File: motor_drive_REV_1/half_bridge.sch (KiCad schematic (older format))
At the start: 28 parts

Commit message: work on component libraries and schematic
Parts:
- removed Q? (x8): Q_NMOS_DGS, symbol Device:Q_NMOS_DGS
- removed R? (x16): 6.8, symbol Device:R
- removed R? (x4): R, symbol Device:R
- added Q? (x2): nmos, symbol motor_drive:nmos
- added R? (x2): R, symbol motor_drive:R
- added R?: R_Shunt, symbol motor_drive:R_Shunt
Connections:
- net labels added: DC_neg, DC_pos
- net labels removed: DC+, DC-, SL, V_sense_n, V_sense_p
- wire segments 26 -> 16

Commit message: organizing pinout and BOM
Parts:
- removed R?: R_Shunt, symbol motor_drive:R_Shunt
- added R3: R, motor_drive_footprints:C_0603_1608Metric, symbol motor_drive:R
- Q1, Q2: renamed from Q?; footprint (none) -> motor_drive_footprints:NTTGS5820NL-D
- R1, R2: renamed from R?; footprint (none) -> motor_drive_footprints:C_0603_1608Metric
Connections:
- wire segments 16 -> 15
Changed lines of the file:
@@
 $Descr A4 11693 8268
 encoding utf-8
-Sheet 3 14
+Sheet 4 14
 Title ""
 Date ""
@@
 Comment4 ""
 $EndDescr
-Wire Wire Line
-	5100 3600 5100 3700
 Connection ~ 5100 3700
 Wire Wire Line
@@
 Text HLabel 5750 3400 1    50   Input ~ 0
 I_sense_p
-Text HLabel 5950 3400 1    50   Input ~ 0
+Text HLabel 6050 3400 1    50   Input ~ 0
 I_sense_n
-Text HLabel 4200 3400 0    50   Input ~ 0
-GH
 Text HLabel 4200 4000 0    50   Input ~ 0
 GL
@@
 Wire Wire Line
 	4200 3700 5100 3700
-Wire Wire Line
-	4250 4000 4400 4000
 Text HLabel 6750 3700 2    50   Input ~ 0
 M
 Text HLabel 5750 3400 1    50   Input ~ 0
 I_sense_p
-Text HLabel 5950 3400 1    50   Input ~ 0
+Text HLabel 6050 3400 1    50   Input ~ 0
 I_sense_n
-Text HLabel 4200 3400 0    50   Input ~ 0
-GH
 Text HLabel 4200 4000 0    50   Input ~ 0
 GL
@@
 Text HLabel 5750 3400 1    50   Input ~ 0
 I_sense_p
-Text HLabel 5950 3400 1    50   Input ~ 0
+Text HLabel 6050 3400 1    50   Input ~ 0
 I_sense_n
-Text HLabel 4200 3400 0    50   Input ~ 0
-GH
 Text HLabel 4200 4000 0    50   Input ~ 0
 GL
@@
 Text HLabel 5750 3400 1    50   Input ~ 0
 I_sense_p
-Text HLabel 5950 3400 1    50   Input ~ 0
+Text HLabel 6050 3400 1    50   Input ~ 0
 I_sense_n
-Text HLabel 4200 3400 0    50   Input ~ 0
-GH
 Text HLabel 4200 4000 0    50   Input ~ 0
 GL
@@
 M
 $Comp
-L motor_drive:nmos Q?
+L motor_drive:nmos Q1
 U 1 1 5E277B3C
 P 5000 3400
-F 0 "Q?" H 5204 3446 50  0000 L CNN
+AR Path="/5E257703/5E277B3C" Ref="Q1"  Part="1"
+AR Path="/5E26944C/5E277B3C" Ref="Q3"  Part="1"
+AR Path="/5E26B60E/5E277B3C" Ref="Q5"  Part="1"
+F 0 "Q5" H 5204 3446 50  0000 L CNN
 F 1 "nmos" H 5204 3355 50  0000 L CNN
-F 2 "" H 5200 3500 50  0001 C CNN
+F 2 "motor_drive_footprints:NTTGS5820NL-D" H 5200 3500 50  0001 C CNN
 F 3 "~" H 5000 3400 50  0001 C CNN
 	1    5000 3400
 	1    0    0    -1
 $EndComp
-Wire Wire Line
-	5100 3650 5100 3700
 $Comp
-L motor_drive:nmos Q?
+L motor_drive:nmos Q2
 U 1 1 5E279347
 P 5000 4000
-F 0 "Q?" H 5204 4046 50  0000 L CNN
+AR Path="/5E257703/5E279347" Ref="Q2"  Part="1"
+AR Path="/5E26944C/5E279347" Ref="Q4"  Part="1"
+AR Path="/5E26B60E/5E279347" Ref="Q6"  Part="1"
+F 0 "Q6" H 5204 4046 50  0000 L CNN
 F 1 "nmos" H 5204 3955 50  0000 L CNN
-F 2 "" H 5200 4100 50  0001 C CNN
+F 2 "motor_drive_footprints:NTTGS5820NL-D" H 5200 4100 50  0001 C CNN
 F 3 "~" H 5000 4000 50  0001 C CNN
 	1    5000 4000
@@
 $EndComp
 $Comp
-L motor_drive:R R?
+L motor_drive:R R2
 U 1 1 5E27A2EF
 P 4550 4000
-F 0 "R?" V 4343 4000 50  0000 C CNN
+AR Path="/5E257703/5E27A2EF" Ref="R2"  Part="1"
+AR Path="/5E26944C/5E27A2EF" Ref="R5"  Part="1"
+AR Path="/5E26B60E/5E27A2EF" Ref="R8"  Part="1"
+F 0 "R8" V 4343 4000 50  0000 C CNN
 F 1 "R" V 4434 4000 50  0000 C CNN
-F 2 "" V 4480 4000 50  0001 C CNN
+F 2 "motor_drive_footprints:C_0603_1608Metric" V 4480 4000 50  0001 C CNN
 F 3 "~" H 4550 4000 50  0001 C CNN
 	1    4550 4000
 	0    1    1    0
 $EndComp
-Wire Wire Line
-	4250 3400 4400 3400
 $Comp
-L motor_drive:R R?
+L motor_drive:R R1
 U 1 1 5E27D5F7
 P 4550 3400
-F 0 "R?" V 4343 3400 50  0000 C CNN
+AR Path="/5E257703/5E27D5F7" Ref="R1"  Part="1"
+AR Path="/5E26944C/5E27D5F7" Ref="R4"  Part="1"
+AR Path="/5E26B60E/5E27D5F7" Ref="R7"  Part="1"
+F 0 "R7" V 4343 3400 50  0000 C CNN
 F 1 "R" V 4434 3400 50  0000 C CNN
-F 2 "" V 4480 3400 50  0001 C CNN
+F 2 "motor_drive_footprints:C_0603_1608Metric" V 4480 3400 50  0001 C CNN
 F 3 "~" H 4550 3400 50  0001 C CNN
 	1    4550 3400
@@
 Wire Wire Line
 	4700 4000 4800 4000
-$Comp
-L motor_drive:R_Shunt R?
-U 1 1 5E27E460
-P 5850 3700
-F 0 "R?" V 5717 3700 50  0000 C CNN
-F 1 "R_Shunt" V 5626 3700 50  0000 C CNN
-F 2 "" V 5780 3700 50  0001 C CNN
-F 3 "~" H 5850 3700 50  0001 C CNN
-	1    5850 3700
-	0    -1   -1   0
-$EndComp
-Wire Wire Line
-	5100 3700 5650 3700
 Wire Wire Line
 	6050 3700 6750 3700
-Wire Wire Line
-	5750 3400 5750 3550
-Wire Wire Line
-	5950 3400 5950 3550
-Text HLabel 4250 4300 0    50   Input ~ 0
+Text HLabel 4200 4300 0    50   Input ~ 0
 DC_neg
-Text HLabel 4250 3100 0    50   Input ~ 0
+Text HLabel 4200 3100 0    50   Input ~ 0
 DC_pos
-Wire Wire Line
-	4250 3100 5100 3100
 Wire Wire Line
 	5100 3100 5100 3200
 Wire Wire Line
-	4250 4300 5100 4300
+	5100 4300 5100 4200
+$Comp
+L motor_drive:R R3
+U 1 1 5E35BEDA
+P 5900 3700
+AR Path="/5E257703/5E35BEDA" Ref="R3"  Part="1"
+AR Path="/5E26944C/5E35BEDA" Ref="R6"  Part="1"
+AR Path="/5E26B60E/5E35BEDA" Ref="R9"  Part="1"
+F 0 "R9" V 5693 3700 50  0000 C CNN
+F 1 "R" V 5784 3700 50  0000 C CNN
+F 2 "motor_drive_footprints:C_0603_1608Metric" V 5830 3700 50  0001 C CNN
+F 3 "~" H 5900 3700 50  0001 C CNN
+	1    5900 3700
+	0    1    1    0
+$EndComp
 Wire Wire Line
-	5100 4300 5100 4200
+	5100 3700 5750 3700
+Wire Wire Line
+	5750 3400 5750 3700
+Connection ~ 5750 3700
+Wire Wire Line
+	6050 3400 6050 3700
+Connection ~ 6050 3700
+Wire Wire Line
+	5100 3700 5100 3600
+Text HLabel 4200 3400 0    50   Input ~ 0
+GH
+Text HLabel 4200 3400 0    50   Input ~ 0
+GH
+Text HLabel 4200 3400 0    50   Input ~ 0
+GH
+Text HLabel 4200 3400 0    50   Input ~ 0
+GH
+Wire Wire Line
+	4200 3400 4400 3400
+Wire Wire Line
+	4200 4000 4400 4000
+Wire Wire Line
+	4200 3100 5100 3100
+Wire Wire Line
+	4200 4300 5100 4300
 $EndSCHEMATC

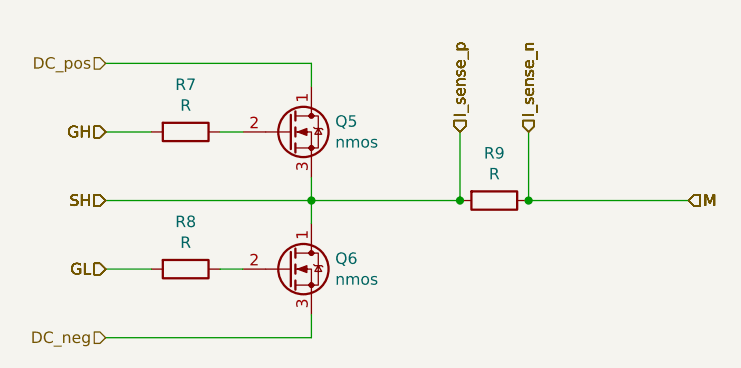
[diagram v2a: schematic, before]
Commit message: working on adding thermistors but encountered too many hierarchicaly copies bug
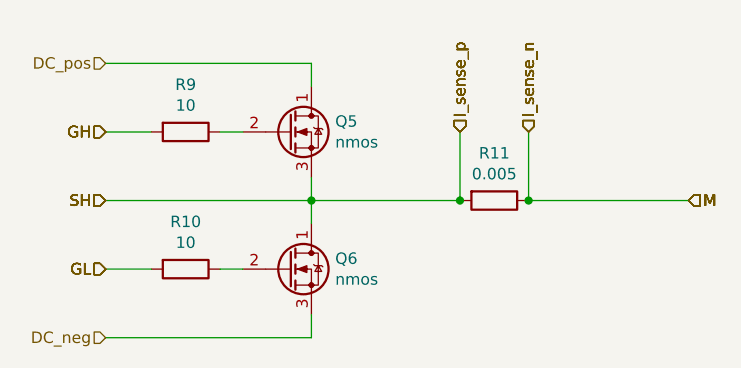
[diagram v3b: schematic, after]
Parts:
- R3: renamed from R1; value R -> 10
- R4: renamed from R2; value R -> 10
- R5: renamed from R3; value R -> 0.005
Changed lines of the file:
@@
 $EndComp
 $Comp
-L motor_drive:R R2
+L motor_drive:R R4
 U 1 1 5E27A2EF
 P 4550 4000
-AR Path="/5E257703/5E27A2EF" Ref="R2"  Part="1"
-AR Path="/5E26944C/5E27A2EF" Ref="R5"  Part="1"
-AR Path="/5E26B60E/5E27A2EF" Ref="R8"  Part="1"
-F 0 "R8" V 4343 4000 50  0000 C CNN
-F 1 "R" V 4434 4000 50  0000 C CNN
+AR Path="/5E257703/5E27A2EF" Ref="R4"  Part="1"
+AR Path="/5E26944C/5E27A2EF" Ref="R7"  Part="1"
+AR Path="/5E26B60E/5E27A2EF" Ref="R10"  Part="1"
+F 0 "R10" V 4343 4000 50  0000 C CNN
+F 1 "10" V 4434 4000 50  0000 C CNN
 F 2 "motor_drive_footprints:C_0603_1608Metric" V 4480 4000 50  0001 C CNN
 F 3 "~" H 4550 4000 50  0001 C CNN
@@
 $EndComp
 $Comp
-L motor_drive:R R1
+L motor_drive:R R3
 U 1 1 5E27D5F7
 P 4550 3400
-AR Path="/5E257703/5E27D5F7" Ref="R1"  Part="1"
-AR Path="/5E26944C/5E27D5F7" Ref="R4"  Part="1"
-AR Path="/5E26B60E/5E27D5F7" Ref="R7"  Part="1"
-F 0 "R7" V 4343 3400 50  0000 C CNN
-F 1 "R" V 4434 3400 50  0000 C CNN
+AR Path="/5E257703/5E27D5F7" Ref="R3"  Part="1"
+AR Path="/5E26944C/5E27D5F7" Ref="R6"  Part="1"
+AR Path="/5E26B60E/5E27D5F7" Ref="R9"  Part="1"
+F 0 "R9" V 4343 3400 50  0000 C CNN
+F 1 "10" V 4434 3400 50  0000 C CNN
 F 2 "motor_drive_footprints:C_0603_1608Metric" V 4480 3400 50  0001 C CNN
 F 3 "~" H 4550 3400 50  0001 C CNN
@@
 	5100 4300 5100 4200
 $Comp
-L motor_drive:R R3
+L motor_drive:R R5
 U 1 1 5E35BEDA
 P 5900 3700
-AR Path="/5E257703/5E35BEDA" Ref="R3"  Part="1"
-AR Path="/5E26944C/5E35BEDA" Ref="R6"  Part="1"
-AR Path="/5E26B60E/5E35BEDA" Ref="R9"  Part="1"
-F 0 "R9" V 5693 3700 50  0000 C CNN
-F 1 "R" V 5784 3700 50  0000 C CNN
+AR Path="/5E257703/5E35BEDA" Ref="R5"  Part="1"
+AR Path="/5E26944C/5E35BEDA" Ref="R8"  Part="1"
+AR Path="/5E26B60E/5E35BEDA" Ref="R11"  Part="1"
+F 0 "R11" V 5693 3700 50  0000 C CNN
+F 1 "0.005" V 5784 3700 50  0000 C CNN
 F 2 "motor_drive_footprints:C_0603_1608Metric" V 5830 3700 50  0001 C CNN
 F 3 "~" H 5900 3700 50  0001 C CNN

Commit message: started layout
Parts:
- removed R5: 0.005, motor_drive_footprints:C_0603_1608Metric, symbol motor_drive:R
- added R6: WSL20101L000FEA18, motor_drive_footprints:WSL20101L000FEA18, symbol motor_drive:WSL20101L000FEA18
- renumbered R3 to R1, R4 to R2
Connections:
- net I_sense_n: now also R6.1
- net I_sense_p: now also R6.2
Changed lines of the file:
@@
 $Descr A4 11693 8268
 encoding utf-8
-Sheet 4 14
+Sheet 4 16
 Title ""
 Date ""
@@
 Text HLabel 5750 3400 1    50   Input ~ 0
 I_sense_p
-Text HLabel 6050 3400 1    50   Input ~ 0
+Text HLabel 6250 3400 1    50   Input ~ 0
 I_sense_n
 Text HLabel 4200 4000 0    50   Input ~ 0
@@
 Wire Wire Line
 	4200 3700 5100 3700
-Text HLabel 6750 3700 2    50   Input ~ 0
+Text HLabel 6950 3700 2    50   Input ~ 0
 M
 Text HLabel 5750 3400 1    50   Input ~ 0
 I_sense_p
-Text HLabel 6050 3400 1    50   Input ~ 0
+Text HLabel 6250 3400 1    50   Input ~ 0
 I_sense_n
 Text HLabel 4200 4000 0    50   Input ~ 0
@@
 Text HLabel 4200 3700 0    50   Input ~ 0
 SH
-Text HLabel 6750 3700 2    50   Input ~ 0
+Text HLabel 6950 3700 2    50   Input ~ 0
 M
 Text HLabel 5750 3400 1    50   Input ~ 0
 I_sense_p
-Text HLabel 6050 3400 1    50   Input ~ 0
+Text HLabel 6250 3400 1    50   Input ~ 0
 I_sense_n
 Text HLabel 4200 4000 0    50   Input ~ 0
@@
 Text HLabel 4200 3700 0    50   Input ~ 0
 SH
-Text HLabel 6750 3700 2    50   Input ~ 0
+Text HLabel 6950 3700 2    50   Input ~ 0
 M
 Text HLabel 5750 3400 1    50   Input ~ 0
 I_sense_p
-Text HLabel 6050 3400 1    50   Input ~ 0
+Text HLabel 6250 3400 1    50   Input ~ 0
 I_sense_n
 Text HLabel 4200 4000 0    50   Input ~ 0
@@
 Text HLabel 4200 3700 0    50   Input ~ 0
 SH
-Text HLabel 6750 3700 2    50   Input ~ 0
+Text HLabel 6950 3700 2    50   Input ~ 0
 M
 $Comp
@@
 $EndComp
 $Comp
-L motor_drive:R R4
+L motor_drive:R R2
 U 1 1 5E27A2EF
 P 4550 4000
-AR Path="/5E257703/5E27A2EF" Ref="R4"  Part="1"
-AR Path="/5E26944C/5E27A2EF" Ref="R7"  Part="1"
-AR Path="/5E26B60E/5E27A2EF" Ref="R10"  Part="1"
-F 0 "R10" V 4343 4000 50  0000 C CNN
+AR Path="/5E257703/5E27A2EF" Ref="R2"  Part="1"
+AR Path="/5E26944C/5E27A2EF" Ref="R5"  Part="1"
+AR Path="/5E26B60E/5E27A2EF" Ref="R8"  Part="1"
+F 0 "R8" V 4343 4000 50  0000 C CNN
 F 1 "10" V 4434 4000 50  0000 C CNN
 F 2 "motor_drive_footprints:C_0603_1608Metric" V 4480 4000 50  0001 C CNN
@@
 $EndComp
 $Comp
-L motor_drive:R R3
+L motor_drive:R R1
 U 1 1 5E27D5F7
 P 4550 3400
-AR Path="/5E257703/5E27D5F7" Ref="R3"  Part="1"
-AR Path="/5E26944C/5E27D5F7" Ref="R6"  Part="1"
-AR Path="/5E26B60E/5E27D5F7" Ref="R9"  Part="1"
-F 0 "R9" V 4343 3400 50  0000 C CNN
+AR Path="/5E257703/5E27D5F7" Ref="R1"  Part="1"
+AR Path="/5E26944C/5E27D5F7" Ref="R4"  Part="1"
+AR Path="/5E26B60E/5E27D5F7" Ref="R7"  Part="1"
+F 0 "R7" V 4343 3400 50  0000 C CNN
 F 1 "10" V 4434 3400 50  0000 C CNN
 F 2 "motor_drive_footprints:C_0603_1608Metric" V 4480 3400 50  0001 C CNN
@@
 	4700 4000 4800 4000
 Wire Wire Line
-	6050 3700 6750 3700
+	6250 3700 6950 3700
 Text HLabel 4200 4300 0    50   Input ~ 0
 DC_neg
@@
 Wire Wire Line
 	5100 4300 5100 4200
-$Comp
-L motor_drive:R R5
-U 1 1 5E35BEDA
-P 5900 3700
-AR Path="/5E257703/5E35BEDA" Ref="R5"  Part="1"
-AR Path="/5E26944C/5E35BEDA" Ref="R8"  Part="1"
-AR Path="/5E26B60E/5E35BEDA" Ref="R11"  Part="1"
-F 0 "R11" V 5693 3700 50  0000 C CNN
-F 1 "0.005" V 5784 3700 50  0000 C CNN
-F 2 "motor_drive_footprints:C_0603_1608Metric" V 5830 3700 50  0001 C CNN
-F 3 "~" H 5900 3700 50  0001 C CNN
-	1    5900 3700
-	0    1    1    0
-$EndComp
 Wire Wire Line
 	5100 3700 5750 3700
 Wire Wire Line
 	5750 3400 5750 3700
-Connection ~ 5750 3700
 Wire Wire Line
-	6050 3400 6050 3700
-Connection ~ 6050 3700
+	6250 3400 6250 3700
 Wire Wire Line
 	5100 3700 5100 3600
@@
 Wire Wire Line
 	4200 4300 5100 4300
+$Comp
+L motor_drive:WSL20101L000FEA18 R6
+U 1 1 5E424CCF
+P 5750 3700
+AR Path="/5E26944C/5E424CCF" Ref="R6"  Part="1"
+AR Path="/5E257703/5E424CCF" Ref="R3"  Part="1"
+AR Path="/5E26B60E/5E424CCF" Ref="R9"  Part="1"
+F 0 "R9" H 6000 3832 60  0000 C CNN
+F 1 "WSL20101L000FEA18" H 6000 3832 60  0001 C CNN
+F 2 "motor_drive_footprints:WSL20101L000FEA18" H 6000 3365 60  0001 C CNN
+F 3 "" H 5750 3700 60  0000 C CNN
+	1    5750 3700
+	1    0    0    -1
+$EndComp
+Connection ~ 5750 3700
+Connection ~ 6250 3700
 $EndSCHEMATC

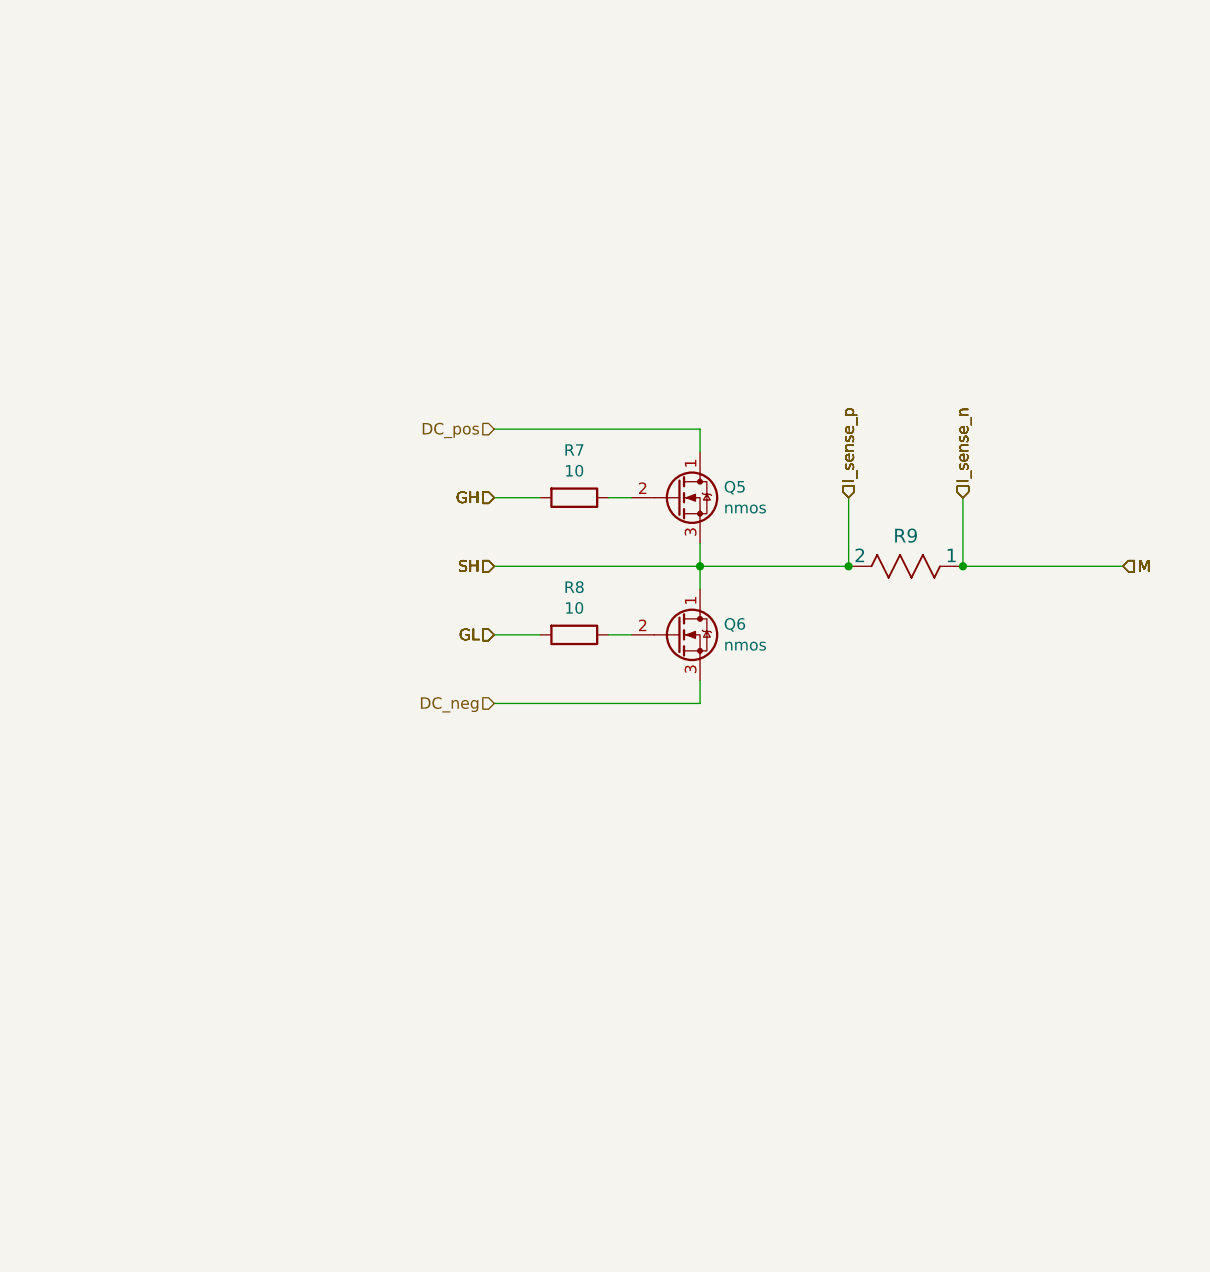
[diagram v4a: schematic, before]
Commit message: gate drive rework and schematic re-organization
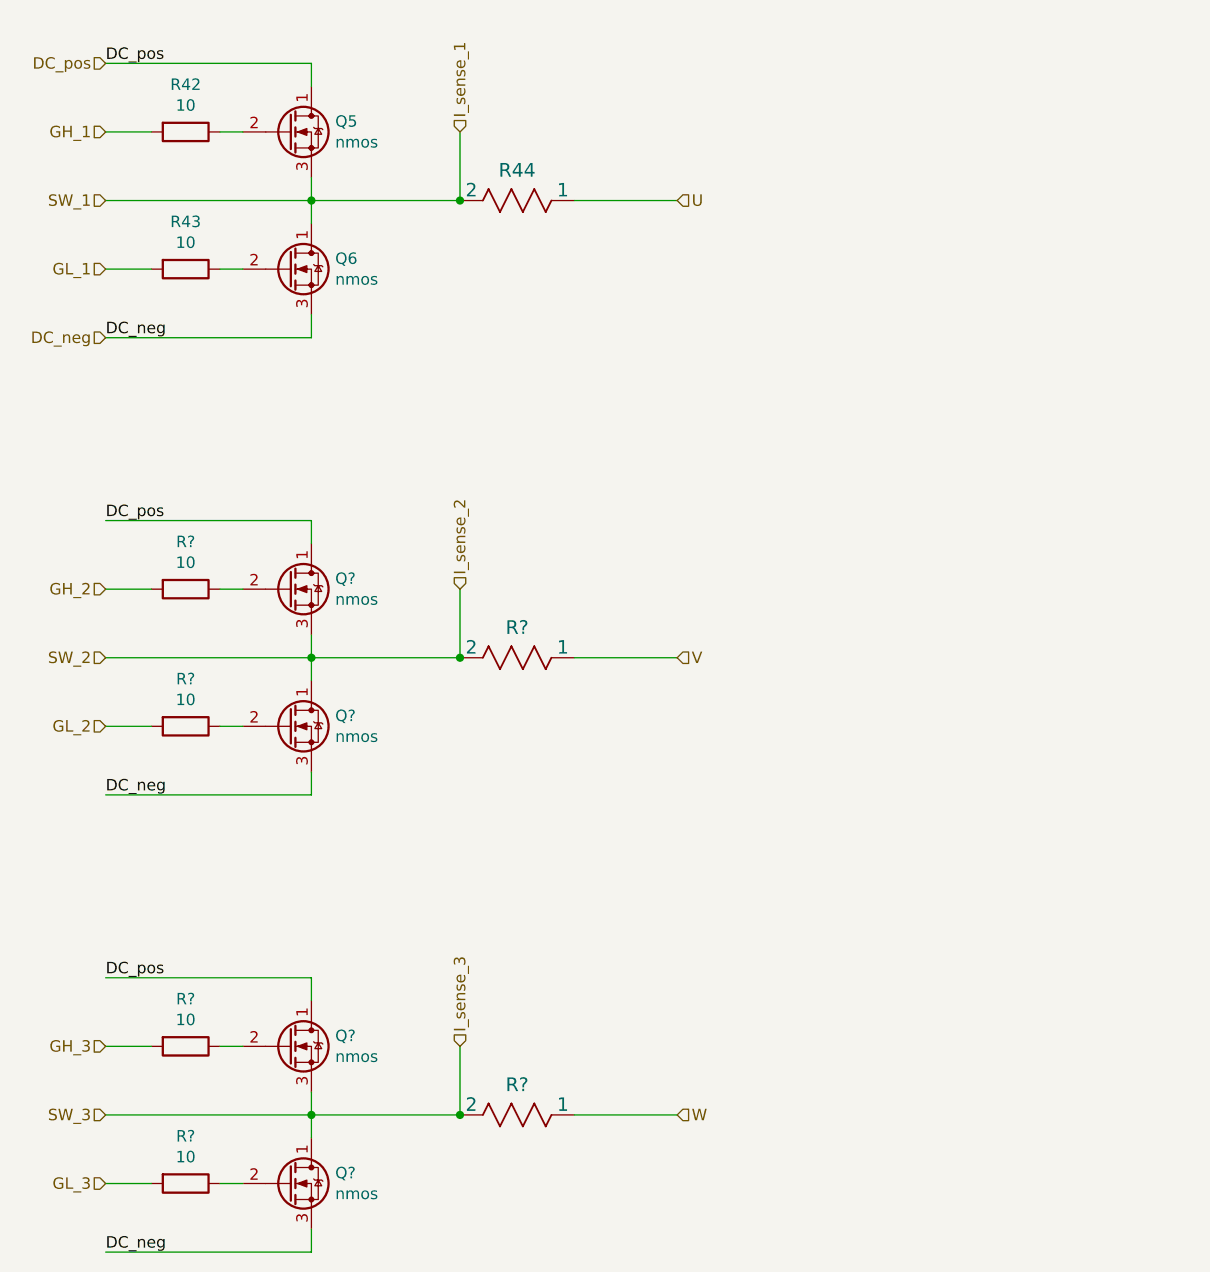
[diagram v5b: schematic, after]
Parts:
- added Q? (x4): nmos, motor_drive_footprints:NTTGS5820NL-D, symbol motor_drive:nmos
- added R? (x4): 10, motor_drive_footprints:C_0603_1608Metric, symbol motor_drive:R
- added R? (x2): WSL20101L000FEA18, motor_drive_footprints:WSL20101L000FEA18, symbol motor_drive:WSL20101L000FEA18
- renumbered Q1 to Q5, Q2 to Q6, R6 to R3, R1 to R42, R2 to R43
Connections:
- net DC_neg: now also Q?.3 (S), Q?.3 (S)
- net DC_pos: now also Q?.1 (D), Q?.1 (D)
- net GH renamed GH_1
- net GL renamed GL_1
- net I_sense_n renamed U
- net I_sense_p renamed I_sense_1
- new net: Q?.2 (G), R?.1 (x4)
- new net GH_2: R?.2
- new net GH_3: R?.2
- new net GL_2: R?.2
- new net GL_3: R?.2
- new net I_sense_2: Q?.1 (D), Q?.3 (S), R?.2
- new net I_sense_3: Q?.1 (D), Q?.3 (S), R?.2
- new net V: R?.1
- new net W: R?.1
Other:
- moved on the sheet: Q5, Q6, R42, R43, R44
